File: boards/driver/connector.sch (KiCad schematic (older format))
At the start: 4 parts, among them J2 Conn_01x24, J3 Conn_01x24, J4 Conn_01x24, J5 Conn_01x24

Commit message: Driver board: significant cleanup. Moved sense amp pairs into a subsheet, split tuning resistors into two globally, pushed input circuits into their corresponding sheets.
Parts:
- J5: renamed from J2; footprint (none) -> Connector_PinHeader_1.00mm:PinHeader_1x24_P1.00mm_Vertical
- J6: renamed from J3; footprint (none) -> Connector_PinHeader_1.00mm:PinHeader_1x24_P1.00mm_Vertical
- J7: renamed from J4; footprint (none) -> Connector_PinHeader_1.00mm:PinHeader_1x24_P1.00mm_Vertical
- J8: renamed from J5; footprint (none) -> Connector_PinHeader_1.00mm:PinHeader_1x24_P1.00mm_Vertical
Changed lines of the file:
@@
 $Descr A4 11693 8268
 encoding utf-8
-Sheet 69 69
+Sheet 77 64
 Title ""
 Date ""
@@
 STR[1..12]
 $Comp
-L Connector_Generic:Conn_01x24 J2
+L Connector_Generic:Conn_01x24 J5
 U 1 1 61D594E4
 P 3050 3200
-F 0 "J2" H 3130 3192 50  0000 L CNN
+F 0 "J5" H 3130 3192 50  0000 L CNN
 F 1 "Conn_01x24" H 3130 3101 50  0000 L CNN
-F 2 "" H 3050 3200 50  0001 C CNN
+F 2 "Connector_PinHeader_1.00mm:PinHeader_1x24_P1.00mm_Vertical" H 3050 3200 50  0001 C CNN
 F 3 "~" H 3050 3200 50  0001 C CNN
 	1    3050 3200
@@
 	2450 3350 2500 3350
 $Comp
-L Connector_Generic:Conn_01x24 J3
+L Connector_Generic:Conn_01x24 J6
 U 1 1 61D62885
 P 4750 3200
-F 0 "J3" H 4830 3192 50  0000 L CNN
+F 0 "J6" H 4830 3192 50  0000 L CNN
 F 1 "Conn_01x24" H 4830 3101 50  0000 L CNN
-F 2 "" H 4750 3200 50  0001 C CNN
+F 2 "Connector_PinHeader_1.00mm:PinHeader_1x24_P1.00mm_Vertical" H 4750 3200 50  0001 C CNN
 F 3 "~" H 4750 3200 50  0001 C CNN
 	1    4750 3200
@@
 	4100 3350 4150 3350
 $Comp
-L Connector_Generic:Conn_01x24 J4
+L Connector_Generic:Conn_01x24 J7
 U 1 1 61D7843B
 P 6600 3200
-F 0 "J4" H 6680 3192 50  0000 L CNN
+F 0 "J7" H 6680 3192 50  0000 L CNN
 F 1 "Conn_01x24" H 6680 3101 50  0000 L CNN
-F 2 "" H 6600 3200 50  0001 C CNN
+F 2 "Connector_PinHeader_1.00mm:PinHeader_1x24_P1.00mm_Vertical" H 6600 3200 50  0001 C CNN
 F 3 "~" H 6600 3200 50  0001 C CNN
 	1    6600 3200
@@
 	6000 2000 6100 2100
 $Comp
-L Connector_Generic:Conn_01x24 J5
+L Connector_Generic:Conn_01x24 J8
 U 1 1 61D85B99
 P 8050 3200
-F 0 "J5" H 8130 3192 50  0000 L CNN
+F 0 "J8" H 8130 3192 50  0000 L CNN
 F 1 "Conn_01x24" H 8130 3101 50  0000 L CNN
-F 2 "" H 8050 3200 50  0001 C CNN
+F 2 "Connector_PinHeader_1.00mm:PinHeader_1x24_P1.00mm_Vertical" H 8050 3200 50  0001 C CNN
 F 3 "~" H 8050 3200 50  0001 C CNN
 	1    8050 3200

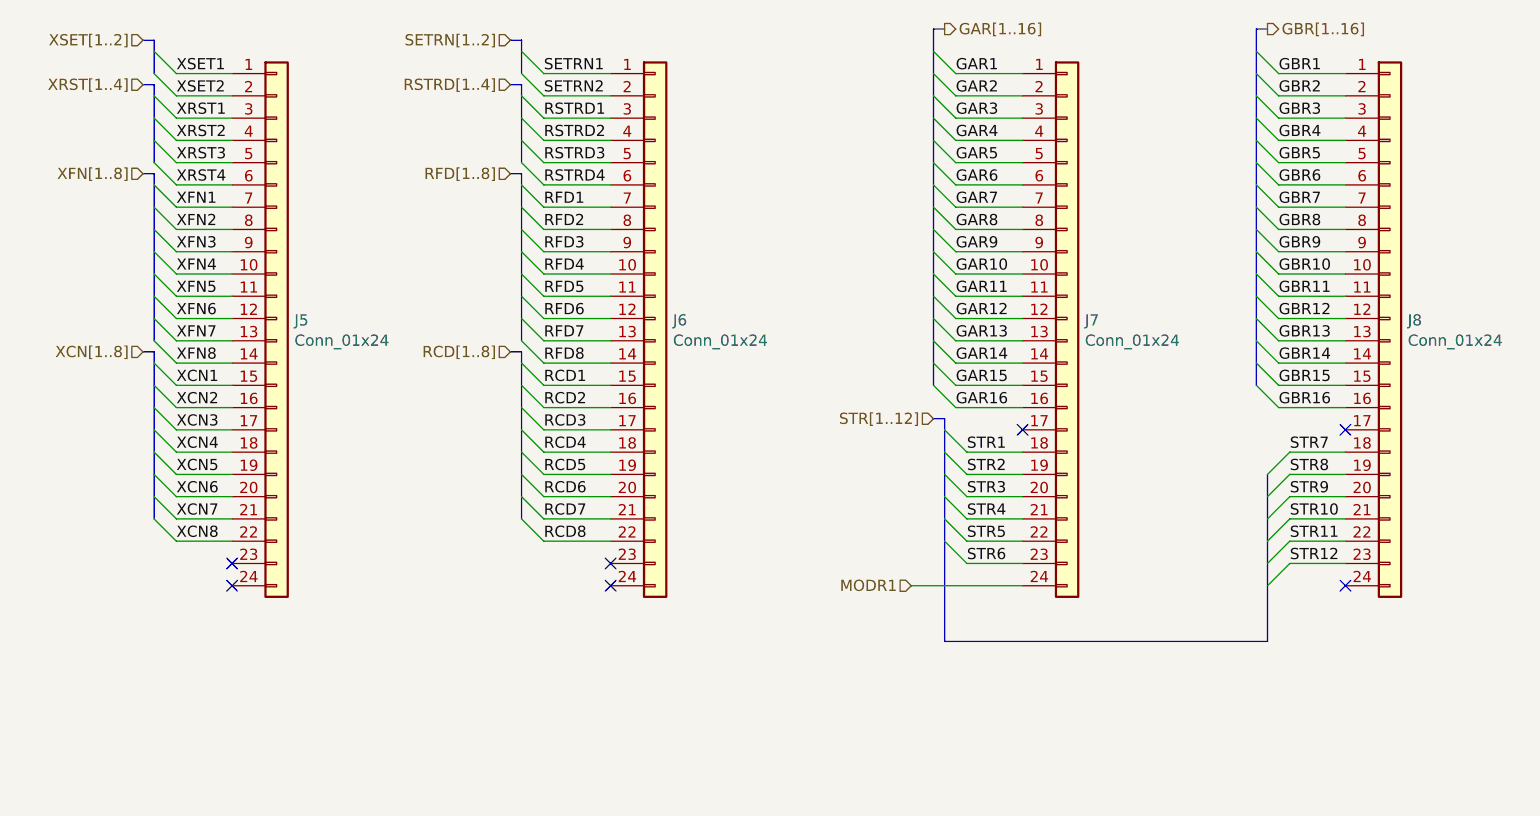
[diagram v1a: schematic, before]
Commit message: Driver board: integrated DIN 41612 backplane connector, and made a dedicated parity inhibit sheet with a different set resistor value.
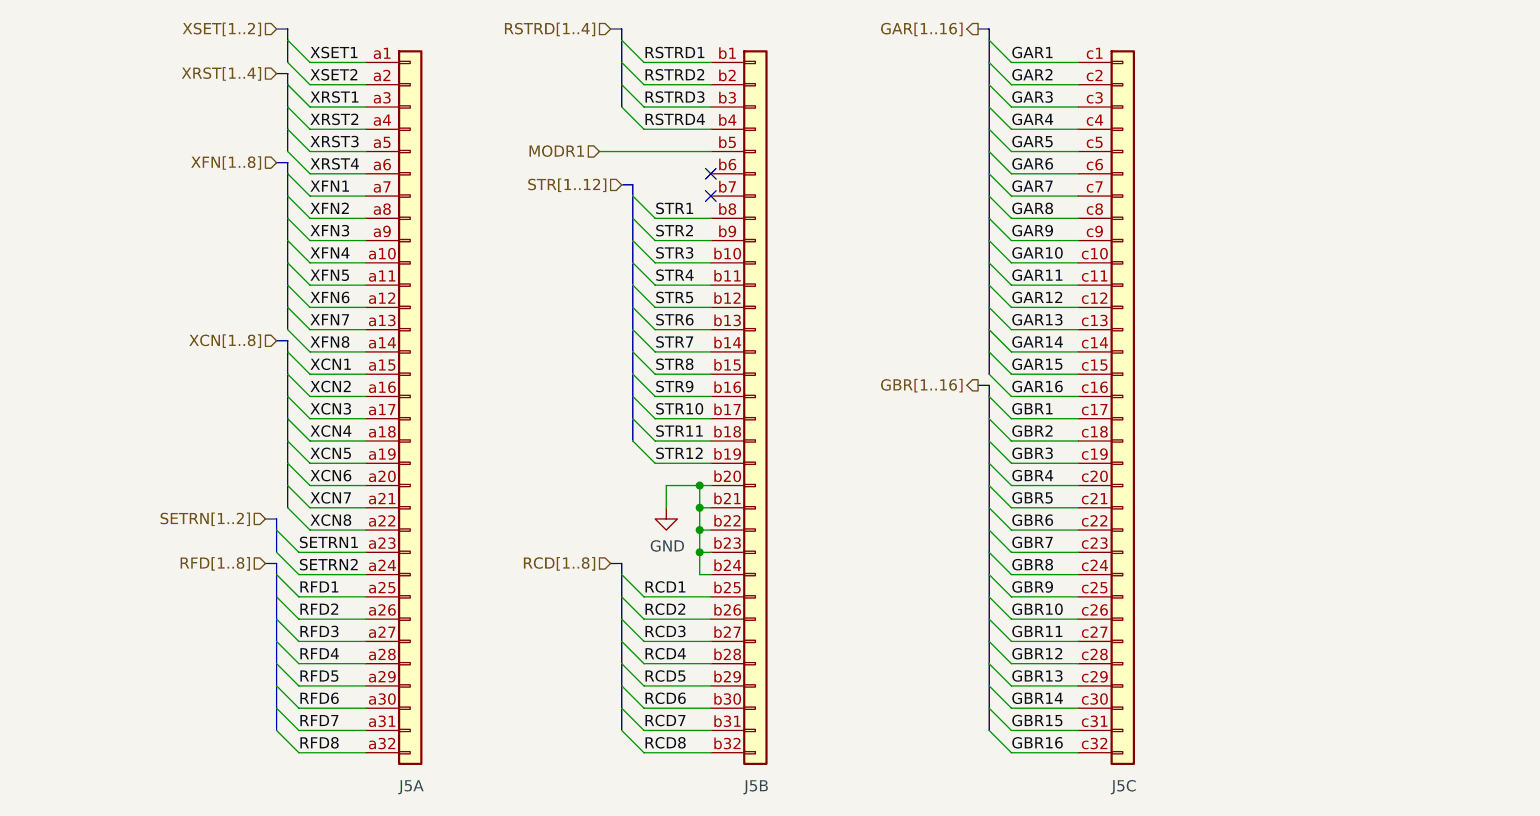
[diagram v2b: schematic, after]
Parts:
- removed J5, J6, J7, J8: Conn_01x24, Connector_PinHeader_1.00mm:PinHeader_1x24_P1.00mm_Vertical, symbol Connector_Generic:Conn_01x24
- added J5: DIN41612_03x32_C, Connector_DIN:DIN41612_C_3x32_Male_Horizontal_THT, symbol lachesis:DIN41612_03x32_C
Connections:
- net GAR1: now also J5.c1
- net GAR10: now also J5.c10
- net GAR11: now also J5.c11
- net GAR12: now also J5.c12
- net GAR13: now also J5.c13
- net GAR14: now also J5.c14
- net GAR15: now also J5.c15
- net GAR16: now also J5.c16
- net GAR2: now also J5.c2
- net GAR3: now also J5.c3
- net GAR4: now also J5.c4
- net GAR5: now also J5.c5
- net GAR6: now also J5.c6
- net GAR7: now also J5.c7
- net GAR8: now also J5.c8
- net GAR9: now also J5.c9
- net GBR1: now also J5.c17
- net GBR10: now also J5.c26
- net GBR11: now also J5.c27
- net GBR12: now also J5.c28
- net GBR13: now also J5.c29
- net GBR14: now also J5.c30
- net GBR15: now also J5.c31
- net GBR16: now also J5.c32
- net GBR2: now also J5.c18
- net GBR3: now also J5.c19
- net GBR4: now also J5.c20
- net GBR5: now also J5.c21
- net GBR6: now also J5.c22
- net GBR7: now also J5.c23
- net GBR8: now also J5.c24
- net GBR9: now also J5.c25
- net MODR1: now also J5.b5
- net RCD1: now also J5.b25
- net RCD2: now also J5.b26
- net RCD3: now also J5.b27
- net RCD4: now also J5.b28
- net RCD5: now also J5.b29
- net RCD6: now also J5.b30
- net RCD7: now also J5.b31
- net RCD8: now also J5.b32
- net RFD1: now also J5.a25
- net RFD2: now also J5.a26
- net RFD3: now also J5.a27
- net RFD4: now also J5.a28
- net RFD5: now also J5.a29
- net RFD6: now also J5.a30
- net RFD7: now also J5.a31
- net RFD8: now also J5.a32
- net RSTRD1: now also J5.b1
- net RSTRD2: now also J5.b2
- net RSTRD3: now also J5.b3
- net RSTRD4: now also J5.b4
- net SETRN1: now also J5.a23
- net SETRN2: now also J5.a24
- net STR1: now also J5.b8
- net STR10: now also J5.b17
- net STR11: now also J5.b18
- net STR12: now also J5.b19
- net STR2: now also J5.b9
- net STR3: now also J5.b10
- net STR4: now also J5.b11
- net STR5: now also J5.b12
- net STR6: now also J5.b13
- net STR7: now also J5.b14
- net STR8: now also J5.b15
- net STR9: now also J5.b16
- net XCN1: now also J5.a15
- net XCN2: now also J5.a16
- net XCN3: now also J5.a17
- net XCN4: now also J5.a18
- net XCN5: now also J5.a19
- net XCN6: now also J5.a20
- net XCN7: now also J5.a21
- net XCN8: now also J5.a22
- net XFN1: now also J5.a7
- net XFN2: now also J5.a8
- net XFN3: now also J5.a9
- net XFN4: now also J5.a10
- net XFN5: now also J5.a11
- net XFN6: now also J5.a12
- net XFN7: now also J5.a13
- net XFN8: now also J5.a14
- net XRST1: now also J5.a3
- net XRST2: now also J5.a4
- net XRST3: now also J5.a5
- net XRST4: now also J5.a6
- net XSET1: now also J5.a1
- net XSET2: now also J5.a2
- new net GND: J5.b20, J5.b21, J5.b22, J5.b23, J5.b24
- no-connect marks 7 -> 2
